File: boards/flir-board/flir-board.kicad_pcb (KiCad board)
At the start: 2 copper layers, 25.5 x 45 mm, 34 parts, among them J101 POWER, J102 I2C, J103 SPI, J104 GPIO3, U101 XC6220B281PR-G, U102 XC6220B301PR-G, U103 XC6222B121PR-G, U104 Flir_LEPTON, X101 ASTMHTE-25.000MHZ-ZJ-E

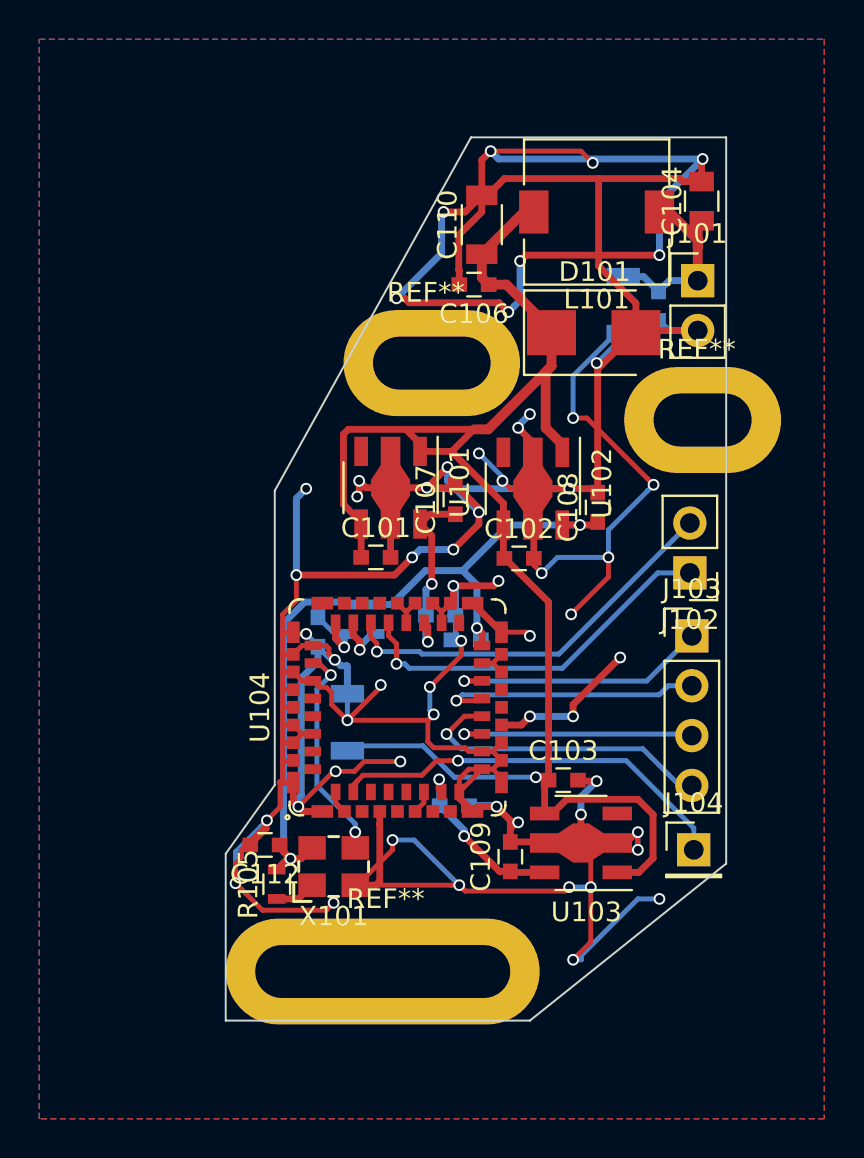
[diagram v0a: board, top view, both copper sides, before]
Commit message: [flir-board] improve board layout
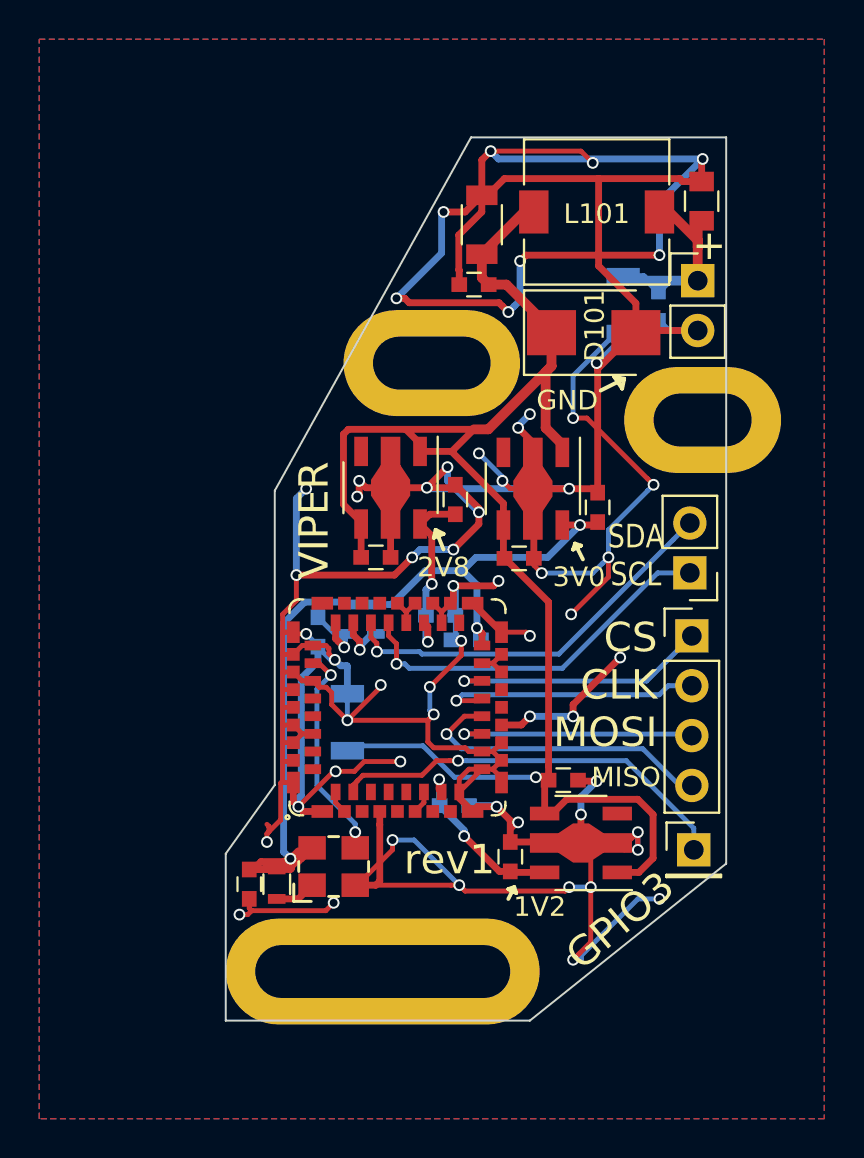
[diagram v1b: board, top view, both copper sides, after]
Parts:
- moved C112 2.15 mm to (145.7, 118.0), turned to 270 degrees
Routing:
- net /3V: track 39.4 -> 50.1 mm
- net GND: track 337.7 -> 329.6 mm
- net /IN_3V3: track 10.4 -> 14.3 mm
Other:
- board text added: "+"
- board text added: "1V2"
- board text added: "2V8"
- board text added: "3V0"
- board text added: "CS CLK MOSI"
- board text added: "CS CLK MOSI MISO"
- board text added: "GND"
- board text added: "GPIO3"
- board text added: "MISO"
- board text added: "RX-VIPER"
- board text added: "Raphael Lehmann"
- board text added: "SDA SCL"
- board text added: "VIPER"
- board text added: "flir-board"
- board text added: "rev1"
